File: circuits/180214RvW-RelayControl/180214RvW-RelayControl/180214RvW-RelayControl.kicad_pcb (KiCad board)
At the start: 2 copper layers, 11 parts, among them J1 Barrel_Jack_Switch, J2 Screw_Terminal_01x02, J3 Screw_Terminal_01x03, K1 G6E, Q1 BC549, U1 LM317_TO3

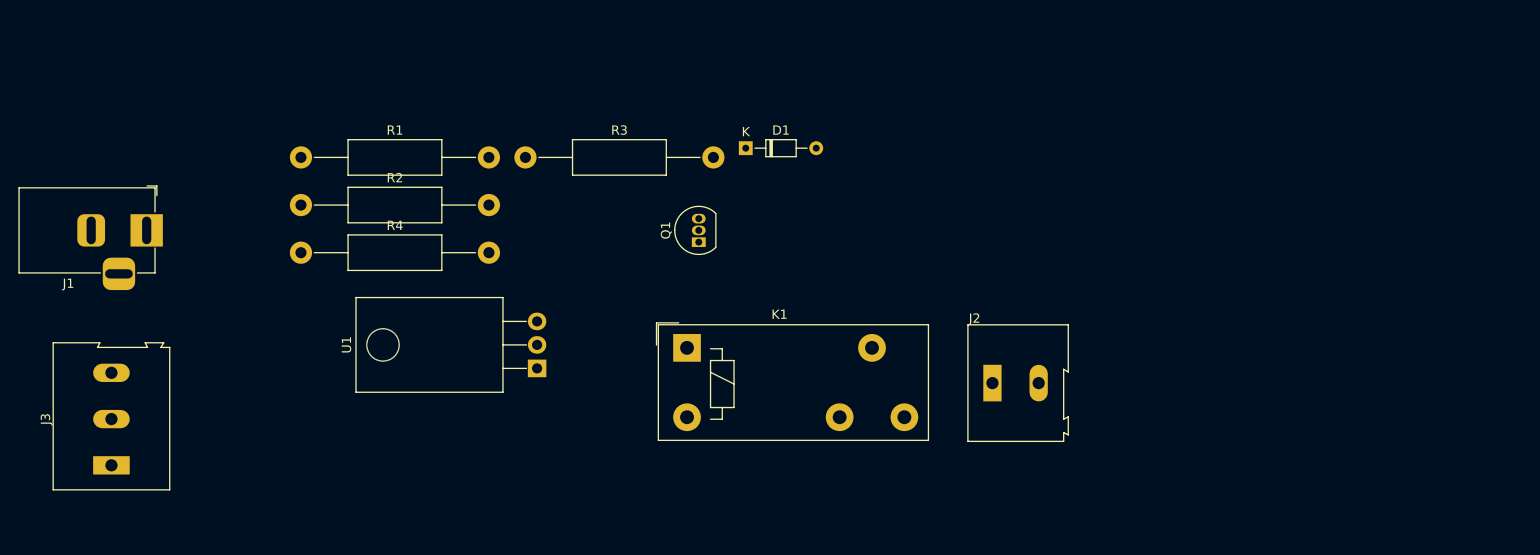
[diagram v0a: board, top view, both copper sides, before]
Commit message: Relay Control board complete
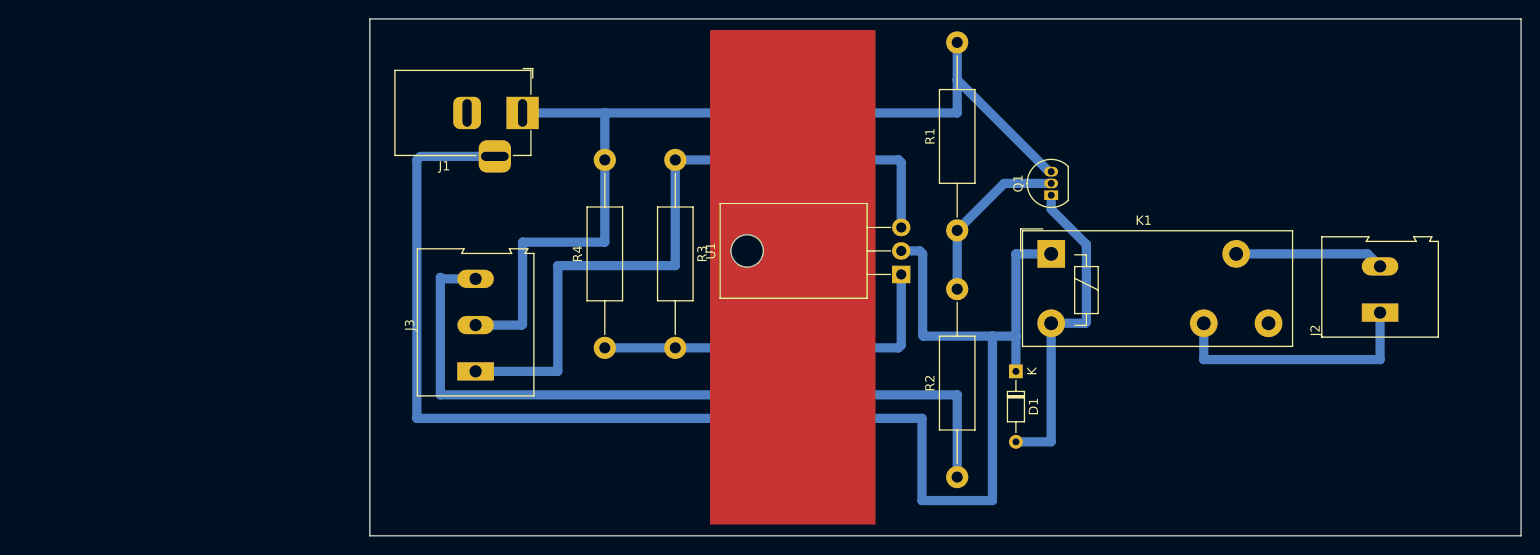
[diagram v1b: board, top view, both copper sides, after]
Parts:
- R1: value 4k7 -> 5k6
- R3: value 240 -> 220
- R4: value 1k5 -> 1k2
- moved R2 76.8 mm to (81.3, 69.8), turned to 90 degrees
- moved R1 71.4 mm to (81.3, 43.2), turned to 90 degrees
- moved J2 42.6 mm to (127.0, 52.1), turned to 90 degrees
- moved J1 42.6 mm to (34.3, 30.5)
- moved J3 40.7 mm to (29.2, 58.4)
- moved U1 40.7 mm to (75.2, 47.9)
- moved K1 40.7 mm to (91.4, 45.7)
- moved Q1 38.4 mm to (91.4, 39.4)
- moved D1 37.9 mm to (87.6, 58.4), turned to 270 degrees
- moved R4 34.4 mm to (43.2, 55.9), turned to 90 degrees
- moved R3 16.2 mm to (50.8, 35.6), turned to 270 degrees
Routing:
- net +12V: track 0.00 -> 163.3 mm
- net GND: track 0.00 -> 105.7 mm
- net Net-(J3-Pad3): track 0.00 -> 81.3 mm
- net Net-(J3-Pad1): track 0.00 -> 76.0 mm
- net Net-(R3-Pad2): track 0.00 -> 39.8 mm
- net Net-(D1-Pad2): track 0.00 -> 35.8 mm
- net Net-(J2-Pad1): track 0.00 -> 28.1 mm
- net Net-(Q1-Pad2): track 0.00 -> 18.6 mm
- net Net-(J2-Pad2): track 0.00 -> 16.1 mm
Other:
- board outline added: 124.5 x 55.9 mm
